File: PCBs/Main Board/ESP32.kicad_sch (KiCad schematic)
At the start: 13 parts, among them U1 19p_Header, U2 Tactile_Button, U3 ESP32_WROOM-32U, U4 19p_Header, U5 0.91_OLED

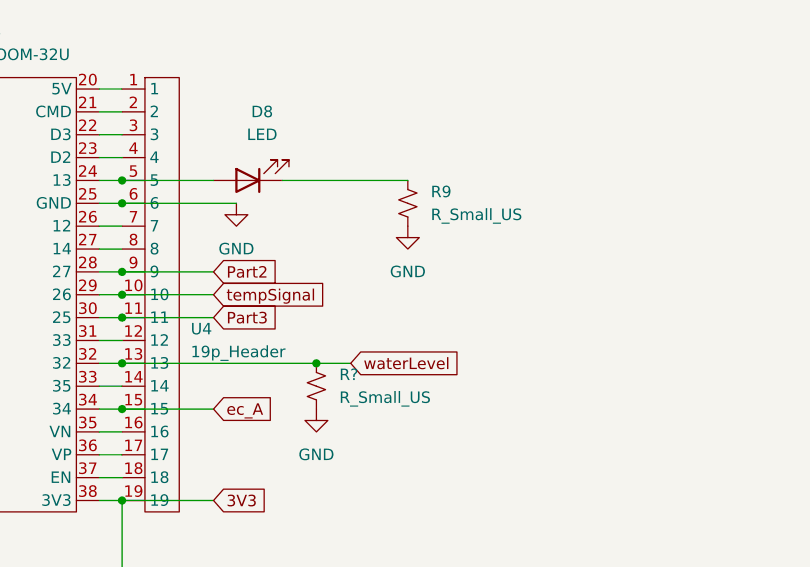
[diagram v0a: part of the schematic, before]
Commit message: changed semaphore wait to ms
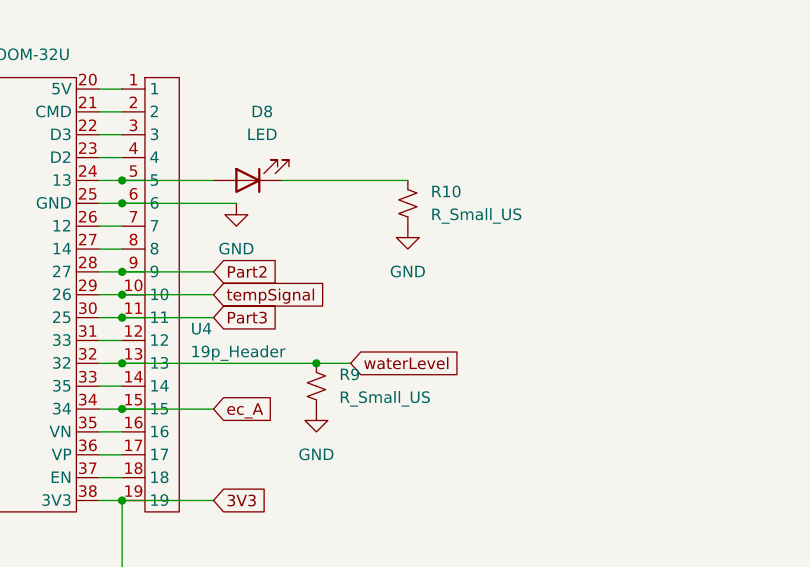
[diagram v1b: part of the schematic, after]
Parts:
- gave numbers to parts that had none: 1
- renumbered R9 to R10
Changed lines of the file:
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@@
   (symbol (lib_id "power:GND") (at 109.22 63.5 0) (unit 1)
     (in_bom yes) (on_board yes) (fields_autoplaced)
-    (property "Reference" "#PWR019" (id 0) (at 109.22 69.85 0)
+    (property "Reference" "#PWR020" (id 0) (at 109.22 69.85 0)
       (effects (font (size 1.27 1.27)) hide)
     )
@@
   (symbol (lib_id "Device:R_Small_US") (at 109.22 60.96 0) (unit 1)
     (in_bom yes) (on_board yes) (fields_autoplaced)
-    (property "Reference" "R9" (id 0) (at 111.76 59.6899 0)
+    (property "Reference" "R10" (id 0) (at 111.76 59.6899 0)
       (effects (font (size 1.27 1.27)) (justify left))
     )
@@
   (symbol (lib_id "Device:R_Small_US") (at 99.06 81.28 0) (unit 1)
     (in_bom yes) (on_board yes) (fields_autoplaced)
-    (property "Reference" "R?" (id 0) (at 101.6 80.0099 0)
+    (property "Reference" "R9" (id 0) (at 101.6 80.0099 0)
       (effects (font (size 1.27 1.27)) (justify left))
     )
@@
   (symbol (lib_id "power:GND") (at 99.06 83.82 0) (unit 1)
     (in_bom yes) (on_board yes) (fields_autoplaced)
-    (property "Reference" "#PWR?" (id 0) (at 99.06 90.17 0)
+    (property "Reference" "#PWR018" (id 0) (at 99.06 90.17 0)
       (effects (font (size 1.27 1.27)) hide)
     )
@@
   (symbol (lib_id "power:GND") (at 105.41 116.84 0) (unit 1)
     (in_bom yes) (on_board yes) (fields_autoplaced)
-    (property "Reference" "#PWR018" (id 0) (at 105.41 123.19 0)
+    (property "Reference" "#PWR019" (id 0) (at 105.41 123.19 0)
       (effects (font (size 1.27 1.27)) hide)
     )

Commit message: Changes to PCB, wired sensors to board
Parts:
- R9: value R_Small_US -> 10k
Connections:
- net at R8.1, U2.4: no longer U2.3
- net at U1.12, U2.1, U3.12 (19): no longer U2.2
- no-connect marks 0 -> 2
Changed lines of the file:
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@@
   (junction (at 77.47 83.82) (diameter 0) (color 0 0 0 0)
   )
-  (junction (at 41.91 123.19) (diameter 0) (color 0 0 0 0)
-  )
   (junction (at 48.26 88.9) (diameter 0) (color 0 0 0 0)
   )
@@
   (junction (at 48.26 68.58) (diameter 0) (color 0 0 0 0)
   )
+  (junction (at 48.26 66.04) (diameter 0) (color 0 0 0 0)
+  )
+  (junction (at 77.47 60.96) (diameter 0) (color 0 0 0 0)
+  )
   (junction (at 48.26 76.2) (diameter 0) (color 0 0 0 0)
   )
-  (junction (at 48.26 66.04) (diameter 0) (color 0 0 0 0)
-  )
-  (junction (at 77.47 60.96) (diameter 0) (color 0 0 0 0)
-  )
   (junction (at 48.26 73.66) (diameter 0) (color 0 0 0 0)
   )
@@
   (junction (at 99.06 78.74) (diameter 0) (color 0 0 0 0)
   )
-  (junction (at 59.69 123.19) (diameter 0) (color 0 0 0 0)
-  )
   (junction (at 77.47 68.58) (diameter 0) (color 0 0 0 0)
   )
@@
   (junction (at 77.47 58.42) (diameter 0) (color 0 0 0 0)
   )
+  (no_connect (at 57.15 120.65))
+  (no_connect (at 41.91 123.19))
   (wire (pts (xy 99.06 78.74) (xy 102.87 78.74))
     (stroke (width 0) (type default) (color 0 0 0 0))
@@
     (stroke (width 0) (type default) (color 0 0 0 0))
   )
+  (wire (pts (xy 59.69 123.19) (xy 59.69 125.73))
+    (stroke (width 0) (type default) (color 0 0 0 0))
+  )
   (wire (pts (xy 77.47 48.26) (xy 74.93 48.26))
     (stroke (width 0) (type default) (color 0 0 0 0))
@@
     (stroke (width 0) (type default) (color 0 0 0 0))
   )
+  (wire (pts (xy 38.1 120.65) (xy 41.91 120.65))
+    (stroke (width 0) (type default) (color 0 0 0 0))
+  )
   (wire (pts (xy 48.26 63.5) (xy 50.8 63.5))
     (stroke (width 0) (type default) (color 0 0 0 0))
@@
     (stroke (width 0) (type default) (color 0 0 0 0))
   )
-  (wire (pts (xy 39.37 76.2) (xy 39.37 125.73))
-    (stroke (width 0) (type default) (color 0 0 0 0))
-  )
-  (wire (pts (xy 41.91 123.19) (xy 41.91 125.73))
-    (stroke (width 0) (type default) (color 0 0 0 0))
-  )
-  (wire (pts (xy 39.37 76.2) (xy 48.26 76.2))
-    (stroke (width 0) (type default) (color 0 0 0 0))
-  )
   (wire (pts (xy 77.47 78.74) (xy 99.06 78.74))
     (stroke (width 0) (type default) (color 0 0 0 0))
@@
     (stroke (width 0) (type default) (color 0 0 0 0))
   )
+  (wire (pts (xy 77.47 55.88) (xy 74.93 55.88))
+    (stroke (width 0) (type default) (color 0 0 0 0))
+  )
+  (wire (pts (xy 48.26 83.82) (xy 50.8 83.82))
+    (stroke (width 0) (type default) (color 0 0 0 0))
+  )
+  (wire (pts (xy 48.26 60.96) (xy 50.8 60.96))
+    (stroke (width 0) (type default) (color 0 0 0 0))
+  )
+  (wire (pts (xy 74.93 60.96) (xy 77.47 60.96))
+    (stroke (width 0) (type default) (color 0 0 0 0))
+  )
+  (wire (pts (xy 48.26 93.98) (xy 49.53 93.98))
+    (stroke (width 0) (type default) (color 0 0 0 0))
+  )
+  (wire (pts (xy 77.47 81.28) (xy 74.93 81.28))
+    (stroke (width 0) (type default) (color 0 0 0 0))
+  )
+  (wire (pts (xy 48.26 76.2) (xy 38.1 76.2))
+    (stroke (width 0) (type default) (color 0 0 0 0))
+  )
+  (wire (pts (xy 35.56 81.28) (xy 48.26 81.28))
+    (stroke (width 0) (type default) (color 0 0 0 0))
+  )
+  (wire (pts (xy 48.26 50.8) (xy 50.8 50.8))
+    (stroke (width 0) (type default) (color 0 0 0 0))
+  )
+  (wire (pts (xy 48.26 76.2) (xy 50.8 76.2))
+    (stroke (width 0) (type default) (color 0 0 0 0))
+  )
+  (wire (pts (xy 31.75 91.44) (xy 48.26 91.44))
+    (stroke (width 0) (type default) (color 0 0 0 0))
+  )
+  (wire (pts (xy 77.47 83.82) (xy 74.93 83.82))
+    (stroke (width 0) (type default) (color 0 0 0 0))
+  )
+  (wire (pts (xy 39.37 73.66) (xy 48.26 73.66))
+    (stroke (width 0) (type default) (color 0 0 0 0))
+  )
+  (wire (pts (xy 77.47 78.74) (xy 74.93 78.74))
+    (stroke (width 0) (type default) (color 0 0 0 0))
+  )
+  (wire (pts (xy 77.47 73.66) (xy 74.93 73.66))
+    (stroke (width 0) (type default) (color 0 0 0 0))
+  )
+  (wire (pts (xy 31.75 88.9) (xy 34.29 88.9))
+    (stroke (width 0) (type default) (color 0 0 0 0))
+  )
+  (wire (pts (xy 77.47 93.98) (xy 77.47 114.3))
+    (stroke (width 0) (type default) (color 0 0 0 0))
+  )
+  (wire (pts (xy 77.47 83.82) (xy 87.63 83.82))
+    (stroke (width 0) (type default) (color 0 0 0 0))
+  )
+  (wire (pts (xy 49.53 78.74) (xy 50.8 78.74))
+    (stroke (width 0) (type default) (color 0 0 0 0))
+  )
+  (wire (pts (xy 48.26 58.42) (xy 50.8 58.42))
+    (stroke (width 0) (type default) (color 0 0 0 0))
+  )
+  (wire (pts (xy 48.26 91.44) (xy 50.8 91.44))
+    (stroke (width 0) (type default) (color 0 0 0 0))
+  )
+  (wire (pts (xy 48.26 78.74) (xy 49.53 78.74))
+    (stroke (width 0) (type default) (color 0 0 0 0))
+  )
+  (wire (pts (xy 39.37 66.04) (xy 48.26 66.04))
+    (stroke (width 0) (type default) (color 0 0 0 0))
+  )
+  (wire (pts (xy 77.47 68.58) (xy 74.93 68.58))
+    (stroke (width 0) (type default) (color 0 0 0 0))
+  )
+  (wire (pts (xy 48.26 81.28) (xy 50.8 81.28))
+    (stroke (width 0) (type default) (color 0 0 0 0))
+  )
+  (wire (pts (xy 77.47 91.44) (xy 74.93 91.44))
+    (stroke (width 0) (type default) (color 0 0 0 0))
+  )
+  (wire (pts (xy 38.1 55.88) (xy 48.26 55.88))
+    (stroke (width 0) (type default) (color 0 0 0 0))
+  )
+  (wire (pts (xy 77.47 114.3) (xy 105.41 114.3))
+    (stroke (width 0) (type default) (color 0 0 0 0))
+  )
   (wire (pts (xy 57.15 123.19) (xy 59.69 123.19))
     (stroke (width 0) (type default) (color 0 0 0 0))
   )
-  (wire (pts (xy 77.47 55.88) (xy 74.93 55.88))
-    (stroke (width 0) (type default) (color 0 0 0 0))
-  )
-  (wire (pts (xy 48.26 83.82) (xy 50.8 83.82))
-    (stroke (width 0) (type default) (color 0 0 0 0))
-  )
-  (wire (pts (xy 48.26 60.96) (xy 50.8 60.96))
-    (stroke (width 0) (type default) (color 0 0 0 0))
-  )
-  (wire (pts (xy 59.69 120.65) (xy 59.69 123.19))
-    (stroke (width 0) (type default) (color 0 0 0 0))
-  )
-  (wire (pts (xy 74.93 60.96) (xy 77.47 60.96))
-    (stroke (width 0) (type default) (color 0 0 0 0))
-  )
-  (wire (pts (xy 48.26 93.98) (xy 49.53 93.98))
-    (stroke (width 0) (type default) (color 0 0 0 0))
-  )
-  (wire (pts (xy 77.47 81.28) (xy 74.93 81.28))
-    (stroke (width 0) (type default) (color 0 0 0 0))
-  )
-  (wire (pts (xy 35.56 81.28) (xy 48.26 81.28))
-    (stroke (width 0) (type default) (color 0 0 0 0))
-  )
-  (wire (pts (xy 48.26 50.8) (xy 50.8 50.8))
-    (stroke (width 0) (type default) (color 0 0 0 0))
-  )
-  (wire (pts (xy 48.26 76.2) (xy 50.8 76.2))
-    (stroke (width 0) (type default) (color 0 0 0 0))
-  )
-  (wire (pts (xy 31.75 91.44) (xy 48.26 91.44))
-    (stroke (width 0) (type default) (color 0 0 0 0))
-  )
-  (wire (pts (xy 77.47 83.82) (xy 74.93 83.82))
-    (stroke (width 0) (type default) (color 0 0 0 0))
-  )
-  (wire (pts (xy 39.37 73.66) (xy 48.26 73.66))
-    (stroke (width 0) (type default) (color 0 0 0 0))
-  )
-  (wire (pts (xy 77.47 78.74) (xy 74.93 78.74))
-    (stroke (width 0) (type default) (color 0 0 0 0))
-  )
-  (wire (pts (xy 77.47 73.66) (xy 74.93 73.66))
-    (stroke (width 0) (type default) (color 0 0 0 0))
-  )
-  (wire (pts (xy 57.15 120.65) (xy 59.69 120.65))
-    (stroke (width 0) (type default) (color 0 0 0 0))
-  )
-  (wire (pts (xy 31.75 88.9) (xy 34.29 88.9))
-    (stroke (width 0) (type default) (color 0 0 0 0))
-  )
-  (wire (pts (xy 77.47 93.98) (xy 77.47 114.3))
-    (stroke (width 0) (type default) (color 0 0 0 0))
-  )
-  (wire (pts (xy 77.47 83.82) (xy 87.63 83.82))
-    (stroke (width 0) (type default) (color 0 0 0 0))
-  )
-  (wire (pts (xy 49.53 78.74) (xy 50.8 78.74))
-    (stroke (width 0) (type default) (color 0 0 0 0))
-  )
-  (wire (pts (xy 48.26 58.42) (xy 50.8 58.42))
-    (stroke (width 0) (type default) (color 0 0 0 0))
-  )
-  (wire (pts (xy 59.69 123.19) (xy 59.69 125.73))
-    (stroke (width 0) (type default) (color 0 0 0 0))
-  )
-  (wire (pts (xy 48.26 91.44) (xy 50.8 91.44))
-    (stroke (width 0) (type default) (color 0 0 0 0))
-  )
-  (wire (pts (xy 48.26 78.74) (xy 49.53 78.74))
-    (stroke (width 0) (type default) (color 0 0 0 0))
-  )
-  (wire (pts (xy 39.37 66.04) (xy 48.26 66.04))
-    (stroke (width 0) (type default) (color 0 0 0 0))
-  )
-  (wire (pts (xy 77.47 68.58) (xy 74.93 68.58))
-    (stroke (width 0) (type default) (color 0 0 0 0))
-  )
-  (wire (pts (xy 48.26 81.28) (xy 50.8 81.28))
-    (stroke (width 0) (type default) (color 0 0 0 0))
-  )
-  (wire (pts (xy 77.47 91.44) (xy 74.93 91.44))
-    (stroke (width 0) (type default) (color 0 0 0 0))
-  )
-  (wire (pts (xy 41.91 120.65) (xy 41.91 123.19))
-    (stroke (width 0) (type default) (color 0 0 0 0))
-  )
-  (wire (pts (xy 38.1 55.88) (xy 48.26 55.88))
-    (stroke (width 0) (type default) (color 0 0 0 0))
-  )
-  (wire (pts (xy 77.47 114.3) (xy 105.41 114.3))
+  (wire (pts (xy 38.1 76.2) (xy 38.1 120.65))
     (stroke (width 0) (type default) (color 0 0 0 0))
   )
@@
   )
   (wire (pts (xy 77.47 53.34) (xy 74.93 53.34))
-    (stroke (width 0) (type default) (color 0 0 0 0))
-  )
-  (wire (pts (xy 41.91 125.73) (xy 39.37 125.73))
     (stroke (width 0) (type default) (color 0 0 0 0))
   )
@@
       (effects (font (size 1.27 1.27)) (justify left))
     )
-    (property "Value" "R_Small_US" (id 1) (at 101.6 82.5499 0)
-      (effects (font (size 1.27 1.27)) (justify left))
-    )
+    (property "Value" "10k" (id 1) (at 101.6 82.5499 0)
+      (effects (font (size 1.27 1.27)) (justify left))
+    )
